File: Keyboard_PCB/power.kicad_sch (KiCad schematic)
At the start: 25 parts, among them U6 ISL91127IRAZ, U7 MCP73833

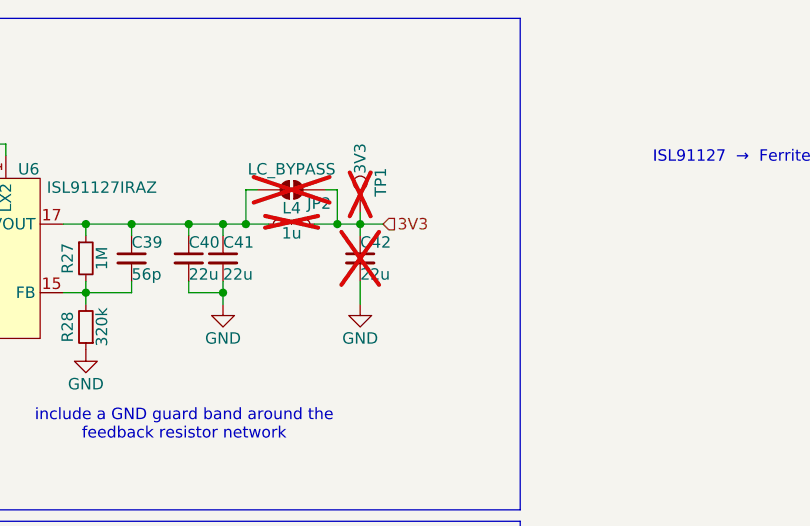
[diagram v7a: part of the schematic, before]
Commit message: Added grid and GND testpoints
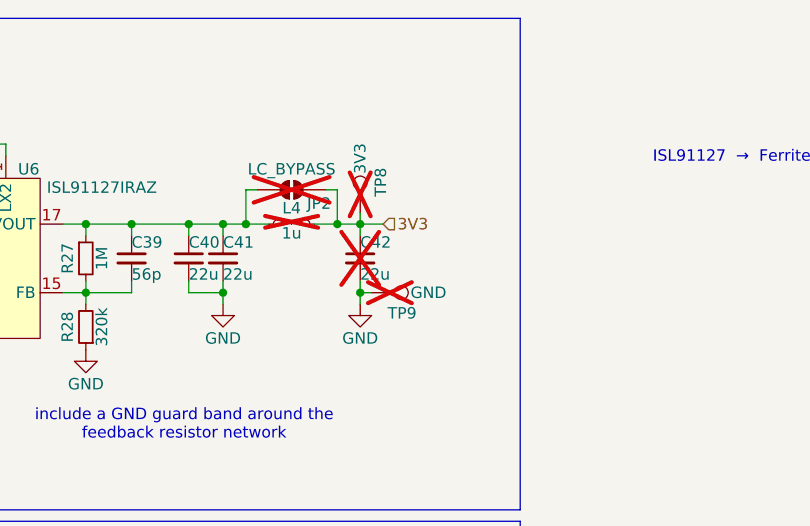
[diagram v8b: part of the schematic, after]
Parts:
- added TP9: GND, TestPoint:TestPoint_Pad_D1.5mm, symbol Connector:TestPoint
- renumbered TP1 to TP8
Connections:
- net GND: now also TP9.1
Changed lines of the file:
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@@
+	)
+	(junction
+		(at 96.52 43.18)
+		(diameter 0)
+		(color 0 0 0 0)
 	)
 	(junction
@@
 	(wire
 		(pts
+			(xy 97.79 43.18) (xy 96.52 43.18)
+		)
+		(stroke
+			(width 0)
+			(type default)
+		)
+	)
+	(wire
+		(pts
 			(xy 44.45 85.09) (xy 49.53 85.09)
 		)
@@
 	(wire
 		(pts
+			(xy 96.52 43.18) (xy 96.52 41.91)
+		)
+		(stroke
+			(width 0)
+			(type default)
+		)
+	)
+	(wire
+		(pts
 			(xy 77.47 80.01) (xy 90.17 80.01)
 		)
@@
 	(wire
 		(pts
-			(xy 96.52 44.45) (xy 96.52 41.91)
+			(xy 96.52 44.45) (xy 96.52 43.18)
 		)
 		(stroke
@@
 		(on_board yes)
 		(dnp yes)
-		(property "Reference" "TP1"
+		(property "Reference" "TP8"
 			(at 98.806 32.512 90)
 			(effects
@@
 			(project "Keyboard_PCB"
 				(path "/dd51e792-c76c-4d43-96de-494177f3b593/700844a0-d855-4a8d-a339-68e2adaa6562"
-					(reference "TP1")
+					(reference "TP8")
 					(unit 1)
 				)
@@
 					(unit 1)
 				)
+			)
+		)
+	)
+	(symbol
+		(lib_id "Connector:TestPoint")
+		(at 97.79 43.18 270)
+		(unit 1)
+		(exclude_from_sim no)
+		(in_bom no)
+		(on_board yes)
+		(dnp yes)
+		(property "Reference" "TP9"
+			(at 99.568 45.466 90)
+			(effects
+				(font
+					(size 1.27 1.27)
+				)
+				(justify left)
+			)
+		)
+		(property "Value" "GND"
+			(at 102.108 43.18 90)
+			(effects
+				(font
+					(size 1.27 1.27)
+				)
+				(justify left)
+			)
+		)
+		(property "Footprint" "TestPoint:TestPoint_Pad_D1.5mm"
+			(at 97.79 48.26 0)
+			(effects
+				(font
+					(size 1.27 1.27)
+				)
+				(hide yes)
+			)
+		)
+		(property "Datasheet" "~"
+			(at 97.79 48.26 0)
+			(effects
+				(font
+					(size 1.27 1.27)
+				)
+				(hide yes)
+			)
+		)
+		(property "Description" "test point"
+			(at 97.79 43.18 0)
+			(effects
+				(font
+					(size 1.27 1.27)
+				)
+				(hide yes)
+			)
+		)
+		(property "mouser" ""
+			(at 97.79 43.18 0)
+			(effects
+				(font
+					(size 1.27 1.27)
+				)
+				(hide yes)
+			)
+		)
+		(property "aliexpress" ""
+			(at 97.79 43.18 90)
+			(effects
+				(font
+					(size 1.27 1.27)
+				)
+				(hide yes)
+			)
+		)
+		(pin "1"
+		)
+		(instances
+			(project "Keyboard_PCB"
+				(path "/dd51e792-c76c-4d43-96de-494177f3b593/700844a0-d855-4a8d-a339-68e2adaa6562"
+					(reference "TP9")
+					(unit 1)
+				)
